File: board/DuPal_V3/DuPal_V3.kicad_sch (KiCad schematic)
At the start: 128 parts, among them J1 ZIF Socket, J2 Debug Header, K1 G6K-2, Q1 2N3904, SW1 RESET, U1 Pico, U10 74HCT166, U11 74HCT166, U12 74HCT166, U13 SN74LV1T125DBV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

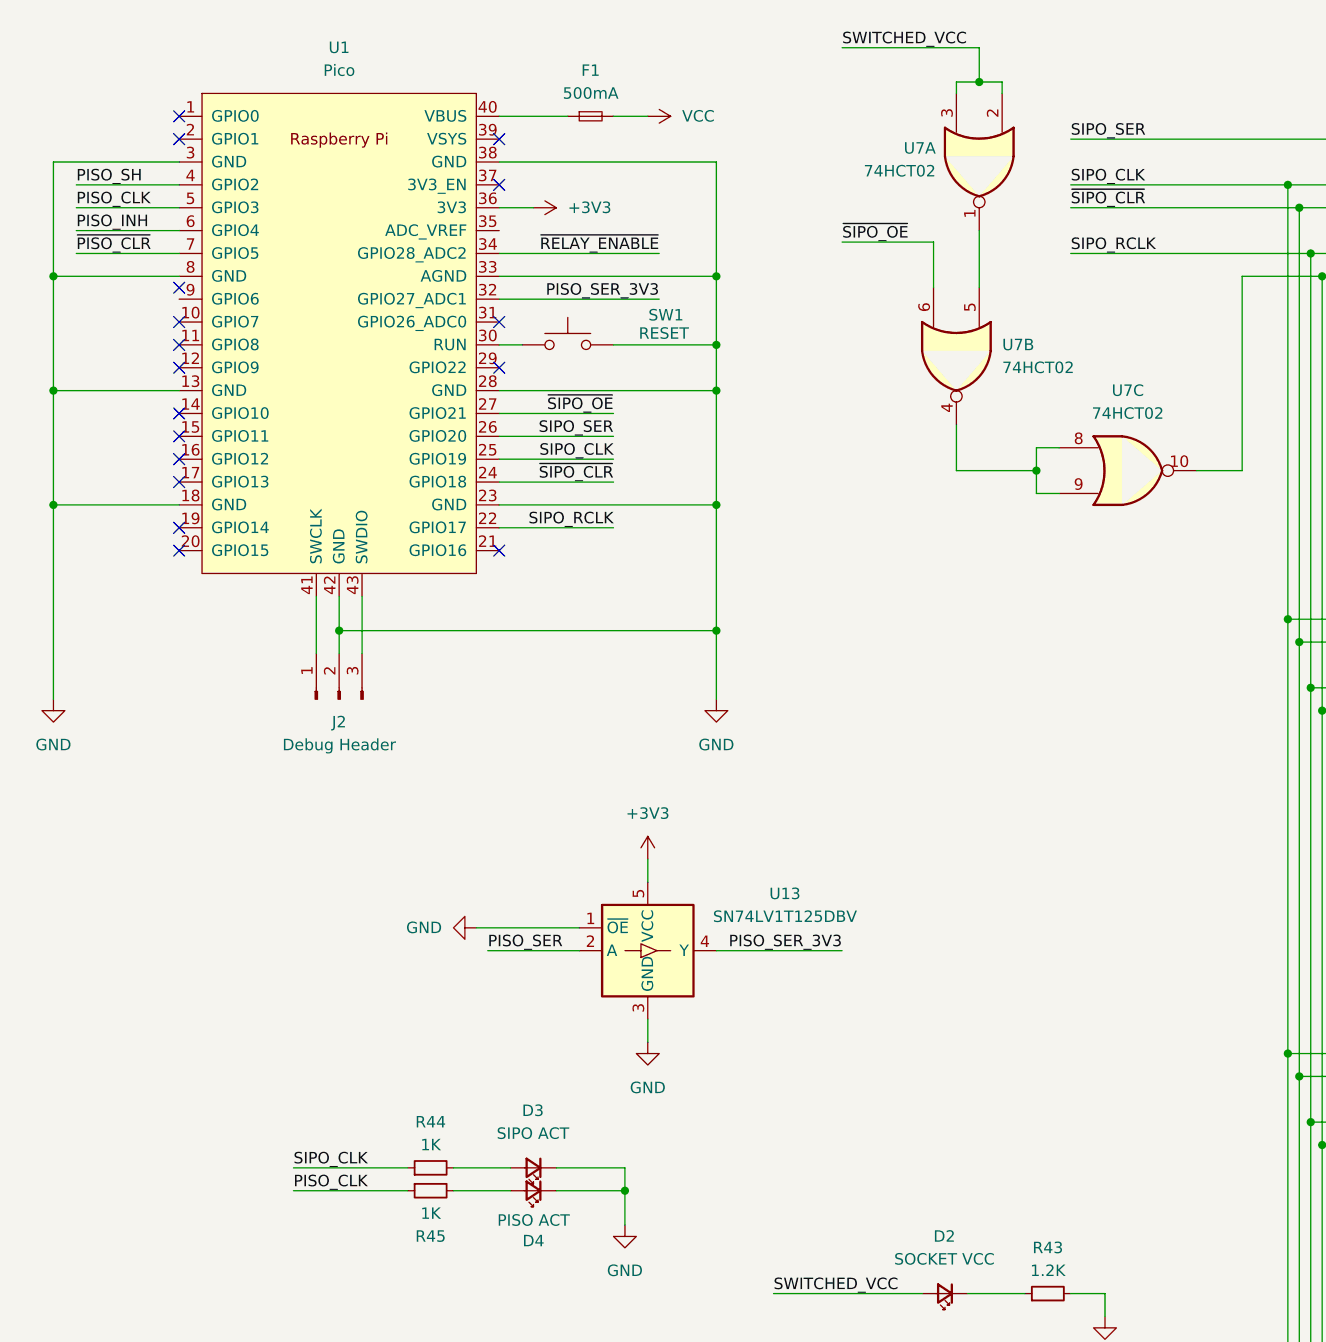
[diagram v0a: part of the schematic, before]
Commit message: First automatic routing of the board
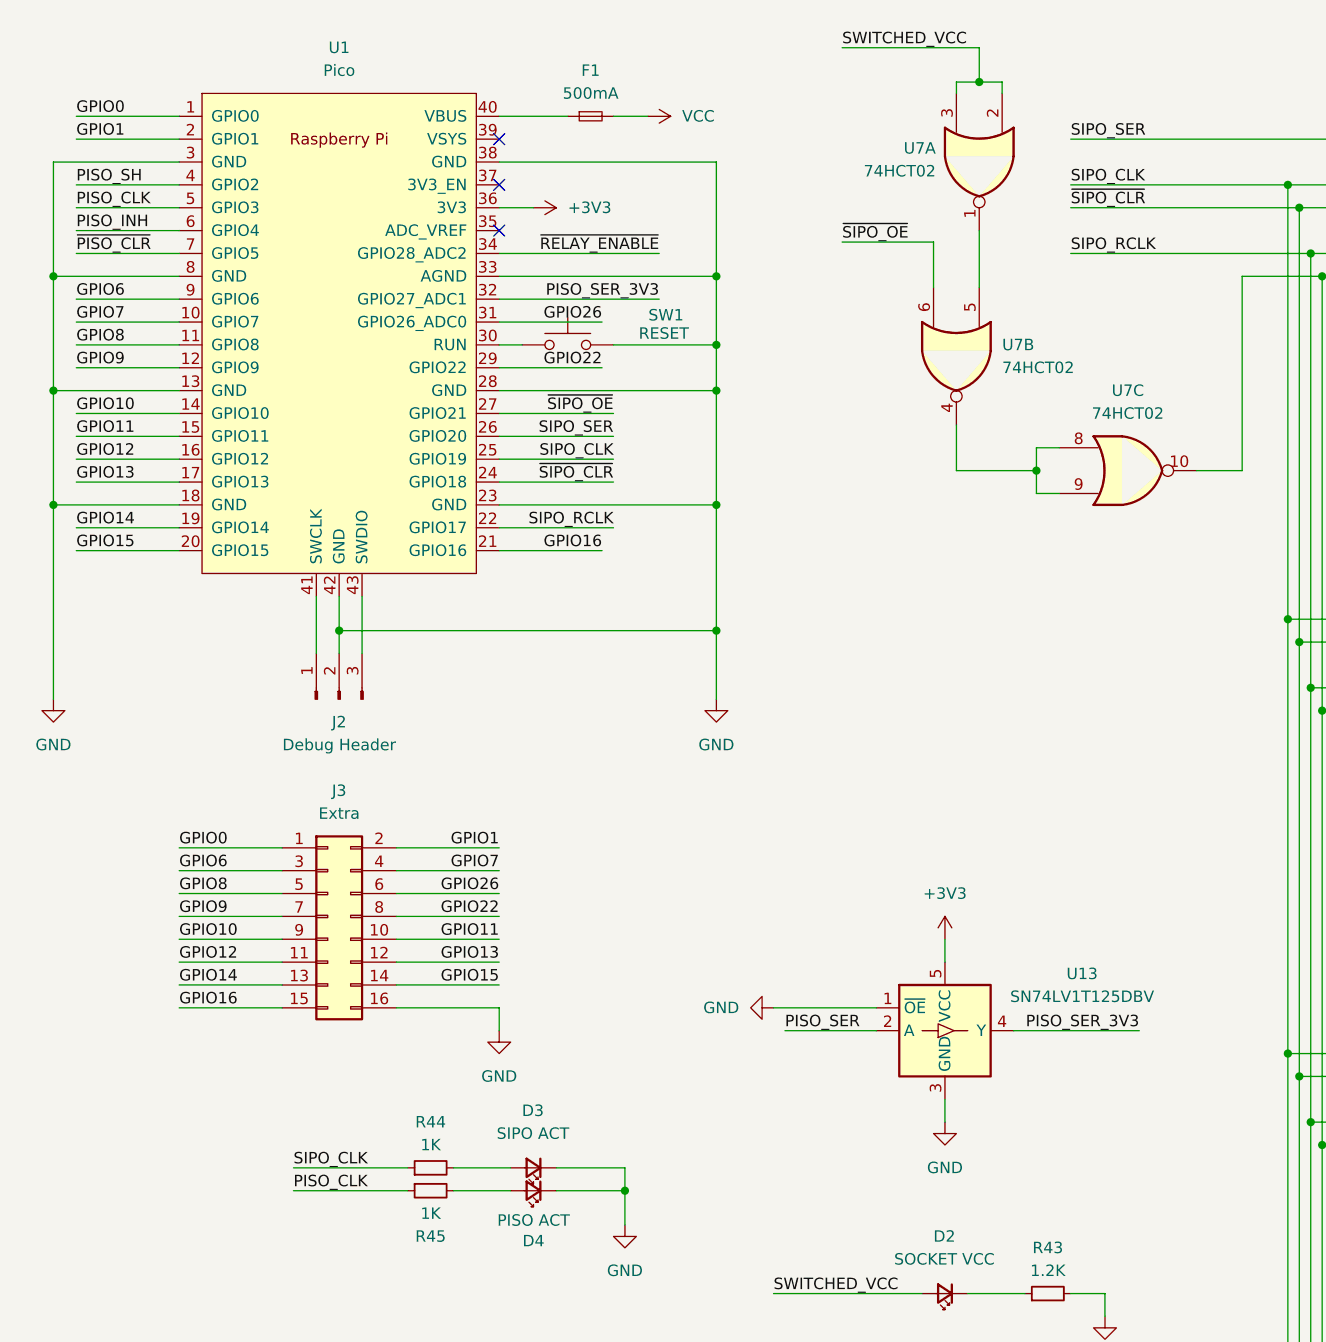
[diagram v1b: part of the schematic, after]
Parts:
- added J3: Extra, Connector_PinHeader_2.54mm:PinHeader_2x08_P2.54mm_Vertical, symbol Connector_Generic:Conn_02x08_Odd_Even
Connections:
- net GND: now also J3.16 (Pin_16)
- net GPIO0: now reaches U1.1 (GPIO0)
- net GPIO0: now also J3.1 (Pin_1)
- net GPIO7: now reaches U1.10 (GPIO7)
- net GPIO7: now also J3.4 (Pin_4)
- net GPIO8: now reaches U1.11 (GPIO8)
- net GPIO8: now also J3.5 (Pin_5)
- net GPIO9: now reaches U1.12 (GPIO9)
- net GPIO9: now also J3.7 (Pin_7)
- net GPIO10: now reaches U1.14 (GPIO10)
- net GPIO10: now also J3.9 (Pin_9)
- net GPIO11: now reaches U1.15 (GPIO11)
- net GPIO11: now also J3.10 (Pin_10)
- net GPIO12: now reaches U1.16 (GPIO12)
- net GPIO12: now also J3.11 (Pin_11)
- net GPIO13: now reaches U1.17 (GPIO13)
- net GPIO13: now also J3.12 (Pin_12)
- net GPIO14: now reaches U1.19 (GPIO14)
- net GPIO14: now also J3.13 (Pin_13)
- net GPIO1: now reaches U1.2 (GPIO1)
- net GPIO1: now also J3.2 (Pin_2)
- net GPIO15: now reaches U1.20 (GPIO15)
- net GPIO15: now also J3.14 (Pin_14)
- net GPIO16: now reaches U1.21 (GPIO16)
- net GPIO16: now also J3.15 (Pin_15)
- net GPIO22: now reaches U1.29 (GPIO22)
- net GPIO22: now also J3.8 (Pin_8)
- net GPIO26: now reaches U1.31 (GPIO26_ADC0)
- net GPIO26: now also J3.6 (Pin_6)
- net GPIO6: now reaches U1.9 (GPIO6)
- net GPIO6: now also J3.3 (Pin_3)
- no-connect marks 20 -> 6
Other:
- moved on the sheet: U13

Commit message: Update silkscreen
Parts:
- R42: value 100K -> 470K
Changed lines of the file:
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@@
 			)
 		)
-		(property "Value" "100K"
+		(property "Value" "470K"
 			(at 115.57 173.9899 0)
 			(effects

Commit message: Add external pullup on /RELAY_ENABLE pin to avoid triggering at powerup
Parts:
- added R86: 10K, Resistor_SMD:R_1206_3216Metric_Pad1.30x1.75mm_HandSolder, symbol Device:R_Small
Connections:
- net +3V3: now also R86.2
- net ~{RELAY_ENABLE}: now also R86.1
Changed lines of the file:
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@@
 	)
 	(junction
+		(at 52.07 264.16)
+		(diameter 0)
+		(color 0 0 0 0)
+	)
+	(junction
 		(at 365.76 147.32)
 		(diameter 0)
@@
 	(wire
 		(pts
+			(xy 52.07 264.16) (xy 54.61 264.16)
+		)
+		(stroke
+			(width 0)
+			(type default)
+		)
+	)
+	(wire
+		(pts
 			(xy 194.31 87.63) (xy 209.55 87.63)
 		)
@@
 	(wire
 		(pts
+			(xy 52.07 273.05) (xy 52.07 264.16)
+		)
+		(stroke
+			(width 0)
+			(type default)
+		)
+	)
+	(wire
+		(pts
 			(xy 161.29 186.69) (xy 161.29 234.95)
 		)
@@
 	(wire
 		(pts
+			(xy 44.45 273.05) (xy 38.1 273.05)
+		)
+		(stroke
+			(width 0)
+			(type default)
+		)
+	)
+	(wire
+		(pts
 			(xy 194.31 36.83) (xy 209.55 36.83)
 		)
@@
 	(wire
 		(pts
-			(xy 38.1 264.16) (xy 54.61 264.16)
+			(xy 38.1 264.16) (xy 52.07 264.16)
 		)
 		(stroke
@@
 	(wire
 		(pts
+			(xy 49.53 273.05) (xy 52.07 273.05)
+		)
+		(stroke
+			(width 0)
+			(type default)
+		)
+	)
+	(wire
+		(pts
 			(xy 227.33 242.57) (xy 236.22 242.57)
 		)
@@
 	(wire
 		(pts
+			(xy 38.1 273.05) (xy 38.1 269.24)
+		)
+		(stroke
+			(width 0)
+			(type default)
+		)
+	)
+	(wire
+		(pts
 			(xy 22.86 57.15) (xy 34.29 57.15)
 		)
@@
 	)
 	(symbol
+		(lib_id "power:+3V3")
+		(at 38.1 269.24 0)
+		(unit 1)
+		(exclude_from_sim no)
+		(in_bom yes)
+		(on_board yes)
+		(dnp no)
+		(property "Reference" "#PWR045"
+			(at 38.1 273.05 0)
+			(effects
+				(font
+					(size 1.27 1.27)
+				)
+				(hide yes)
+			)
+		)
+		(property "Value" "+3V3"
+			(at 34.29 267.462 0)
+			(effects
+				(font
+					(size 1.27 1.27)
+				)
+			)
+		)
+		(property "Footprint" ""
+			(at 38.1 269.24 0)
+			(effects
+				(font
+					(size 1.27 1.27)
+				)
+				(hide yes)
+			)
+		)
+		(property "Datasheet" ""
+			(at 38.1 269.24 0)
+			(effects
+				(font
+					(size 1.27 1.27)
+				)
+				(hide yes)
+			)
+		)
+		(property "Description" "Power symbol creates a global label with name \"+3V3\""
+			(at 38.1 269.24 0)
+			(effects
+				(font
+					(size 1.27 1.27)
+				)
+				(hide yes)
+			)
+		)
+		(pin "1"
+		)
+		(instances
+			(project "DuPal_V3"
+				(path "/cb33c233-8771-4088-8587-4d700b37a618"
+					(reference "#PWR045")
+					(unit 1)
+				)
+			)
+		)
+	)
+	(symbol
 		(lib_id "74xx:74HC595")
 		(at 175.26 36.83 0)
@@
 					(unit 1)
 				)
+			)
+		)
+	)
+	(symbol
+		(lib_id "Device:R_Small")
+		(at 46.99 273.05 270)
+		(unit 1)
+		(exclude_from_sim no)
+		(in_bom yes)
+		(on_board yes)
+		(dnp no)
+		(property "Reference" "R86"
+			(at 46.99 270.764 90)
+			(effects
+				(font
+					(size 1.27 1.27)
+				)
+			)
+		)
+		(property "Value" "10K"
+			(at 46.99 275.082 90)
+			(effects
+				(font
+					(size 1.27 1.27)
+				)
+			)
+		)
+		(property "Footprint" "Resistor_SMD:R_1206_3216Metric_Pad1.30x1.75mm_HandSolder"
+			(at 46.99 273.05 0)
+			(effects
+				(font
+					(size 1.27 1.27)
+				)
+				(hide yes)
+			)
+		)
+		(property "Datasheet" "~"
+			(at 46.99 273.05 0)
+			(effects
+				(font
+					(size 1.27 1.27)
+				)
+				(hide yes)
+			)
+		)
+		(property "Description" "Resistor, small symbol"
+			(at 46.99 273.05 0)
+			(effects
+				(font
+					(size 1.27 1.27)
+				)
+				(hide yes)
+			)
+		)
+		(pin "1"
+		)
+		(pin "2"
+		)
+		(instances
+			(project "DuPal_V3"
+				(path "/cb33c233-8771-4088-8587-4d700b37a618"
+					(reference "R86")
+					(unit 1)
+				)

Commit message: Fix missing connection on a shifter
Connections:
- net PISO_INH: now also U9.6 (CE)
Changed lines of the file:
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@@
 	)
 	(junction
+		(at 224.79 106.68)
+		(diameter 0)
+		(color 0 0 0 0)
+	)
+	(junction
 		(at 321.31 223.52)
 		(diameter 0)
@@
 	(wire
 		(pts
+			(xy 224.79 106.68) (xy 224.79 161.29)
+		)
+		(stroke
+			(width 0)
+			(type default)
+		)
+	)
+	(wire
+		(pts
 			(xy 20.32 88.9) (xy 20.32 67.31)
 		)
@@
 	(wire
 		(pts
-			(xy 224.79 52.07) (xy 224.79 161.29)
+			(xy 224.79 52.07) (xy 224.79 106.68)
 		)
 		(stroke
@@
 		)
 		(stroke
+			(width 0)
+			(type default)
+		)
+	)
+	(wire
+		(pts
+			(xy 224.79 106.68) (xy 236.22 106.68)
+		)
+		(stroke

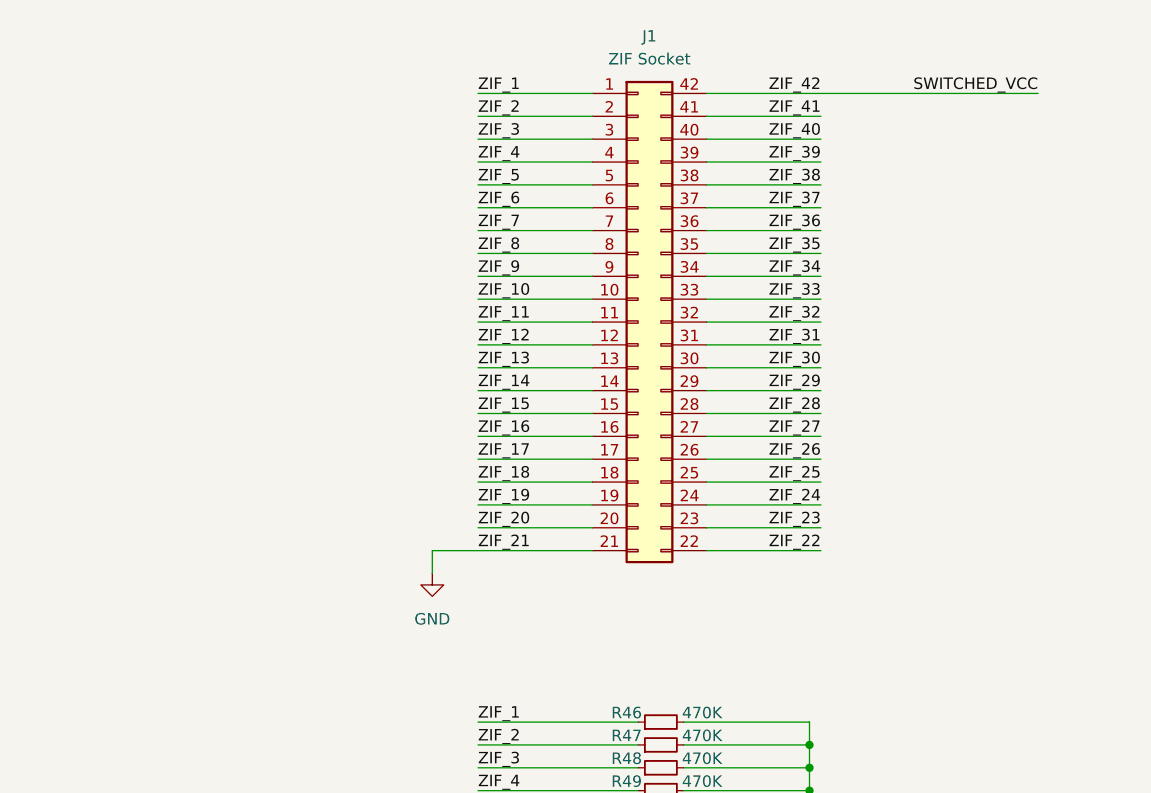
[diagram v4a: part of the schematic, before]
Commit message: Add pinheaders in schematic
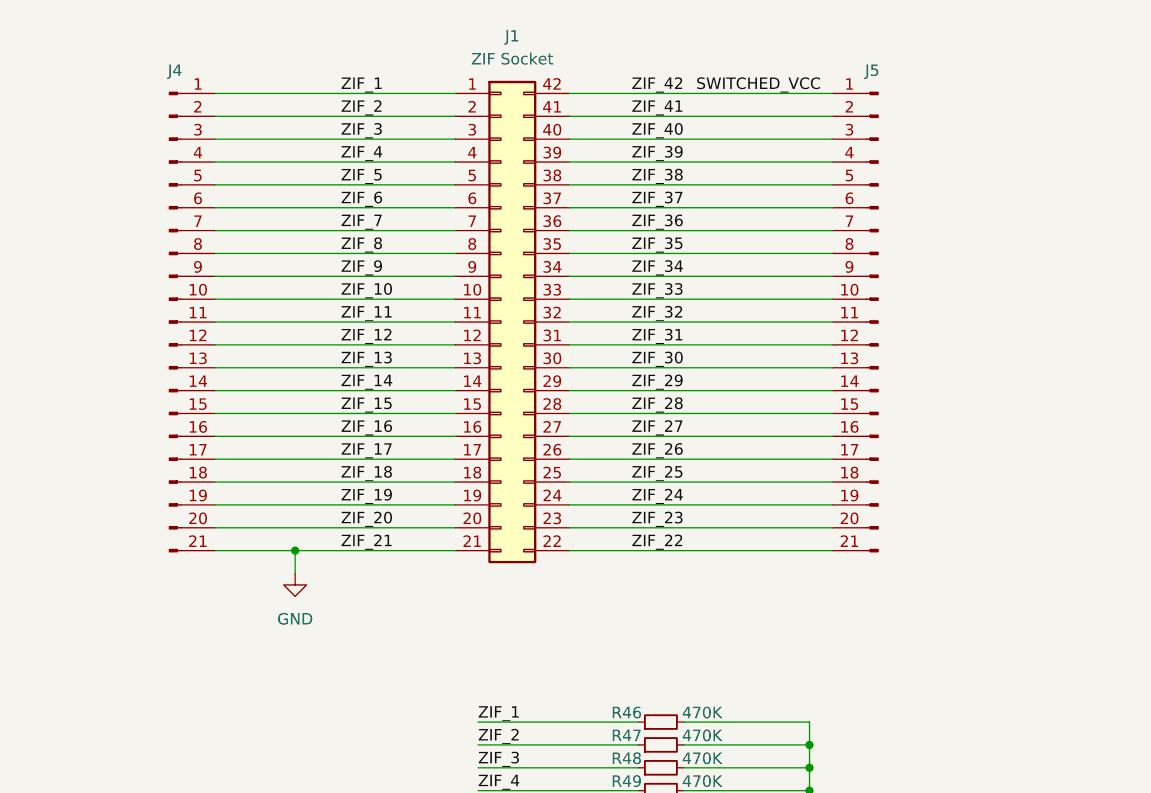
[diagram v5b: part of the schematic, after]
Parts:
- added J4, J5: Conn_01x21_Pin, Connector_PinHeader_2.54mm:PinHeader_1x21_P2.54mm_Vertical, symbol Connector:Conn_01x21_Pin
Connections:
- net GND: now also J4.21 (Pin_21)
- net SWITCHED_VCC: now also J5.1 (Pin_1)
- net ZIF_1: now also J4.1 (Pin_1)
- net ZIF_10: now also J4.10 (Pin_10)
- net ZIF_11: now also J4.11 (Pin_11)
- net ZIF_12: now also J4.12 (Pin_12)
- net ZIF_13: now also J4.13 (Pin_13)
- net ZIF_14: now also J4.14 (Pin_14)
- net ZIF_15: now also J4.15 (Pin_15)
- net ZIF_16: now also J4.16 (Pin_16)
- net ZIF_17: now also J4.17 (Pin_17)
- net ZIF_18: now also J4.18 (Pin_18)
- net ZIF_19: now also J4.19 (Pin_19)
- net ZIF_2: now also J4.2 (Pin_2)
- net ZIF_20: now also J4.20 (Pin_20)
- net ZIF_22: now also J5.21 (Pin_21)
- net ZIF_23: now also J5.20 (Pin_20)
- net ZIF_24: now also J5.19 (Pin_19)
- net ZIF_25: now also J5.18 (Pin_18)
- net ZIF_26: now also J5.17 (Pin_17)
- net ZIF_27: now also J5.16 (Pin_16)
- net ZIF_28: now also J5.15 (Pin_15)
- net ZIF_29: now also J5.14 (Pin_14)
- net ZIF_3: now also J4.3 (Pin_3)
- net ZIF_30: now also J5.13 (Pin_13)
- net ZIF_31: now also J5.12 (Pin_12)
- net ZIF_32: now also J5.11 (Pin_11)
- net ZIF_33: now also J5.10 (Pin_10)
- net ZIF_34: now also J5.9 (Pin_9)
- net ZIF_35: now also J5.8 (Pin_8)
- net ZIF_36: now also J5.7 (Pin_7)
- net ZIF_37: now also J5.6 (Pin_6)
- net ZIF_38: now also J5.5 (Pin_5)
- net ZIF_39: now also J5.4 (Pin_4)
- net ZIF_4: now also J4.4 (Pin_4)
- net ZIF_40: now also J5.3 (Pin_3)
- net ZIF_41: now also J5.2 (Pin_2)
- net ZIF_5: now also J4.5 (Pin_5)
- net ZIF_6: now also J4.6 (Pin_6)
- net ZIF_7: now also J4.7 (Pin_7)
- net ZIF_8: now also J4.8 (Pin_8)
- net ZIF_9: now also J4.9 (Pin_9)
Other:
- moved on the sheet: J1

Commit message: Add pinheaders to rev. 1 V3 board
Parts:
- JP1: footprint Jumper:SolderJumper-2_P1.3mm_Open_RoundedPad1.0x1.5mm -> Jumper:SolderJumper-2_P1.3mm_Bridged_RoundedPad1.0x1.5mm
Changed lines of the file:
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@@
 			)
 		)
-		(property "Footprint" "Jumper:SolderJumper-2_P1.3mm_Open_RoundedPad1.0x1.5mm"
+		(property "Footprint" "Jumper:SolderJumper-2_P1.3mm_Bridged_RoundedPad1.0x1.5mm"
 			(at 109.22 264.16 0)
 			(effects
